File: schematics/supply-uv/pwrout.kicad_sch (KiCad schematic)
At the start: 76 parts, among them Q10 STP13NK60Z, Q11 STP13NK60Z, Q12 IRLML0030, Q7 IRLML0030, Q8 IRLML5203, Q9 IRLML0030, U15 EL817, U16 UC3525, U17 OP213ESZ, U18 IRS21867S, U19 EL817, U20 INA169

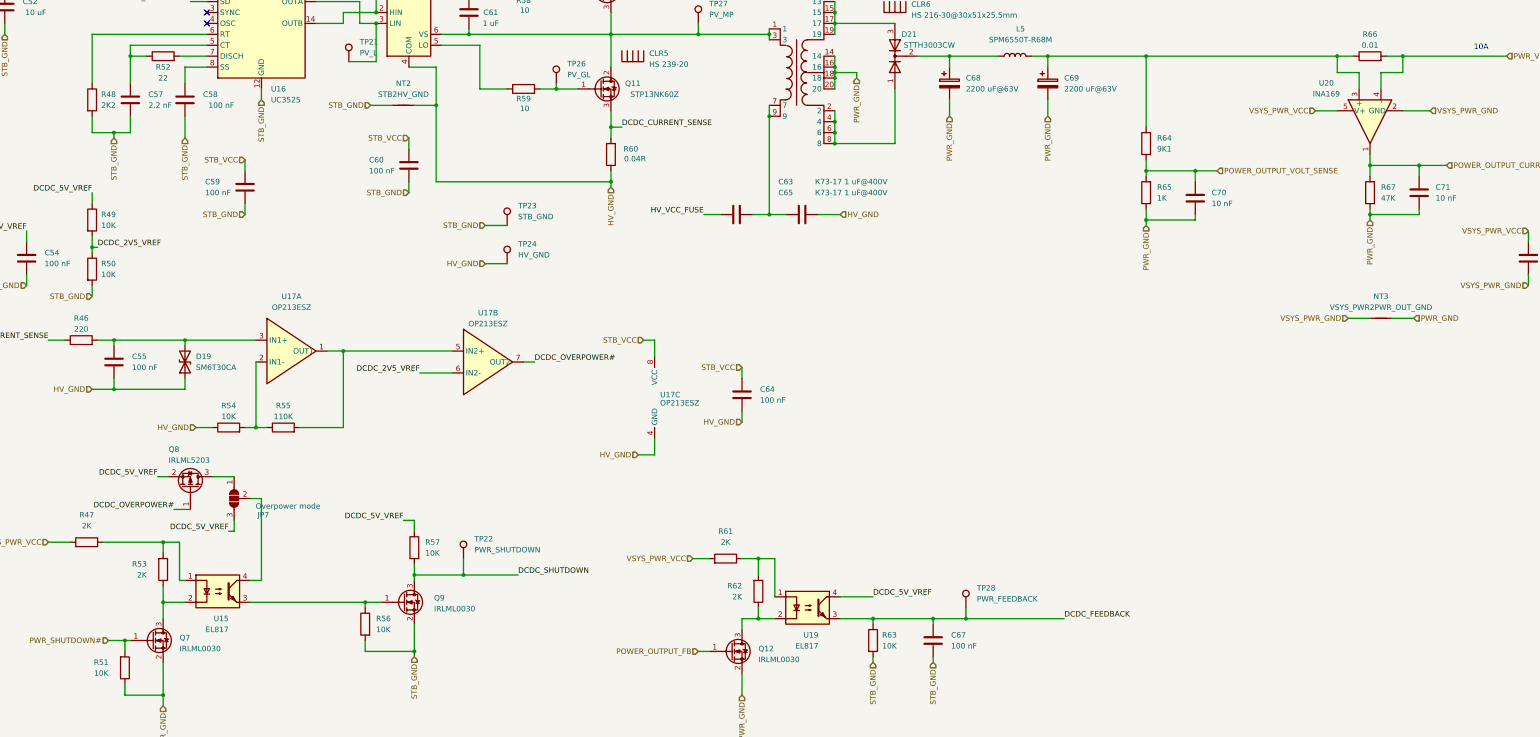
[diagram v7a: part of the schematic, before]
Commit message: power board works (except power output driver, not tested yet), I ready to solder control board
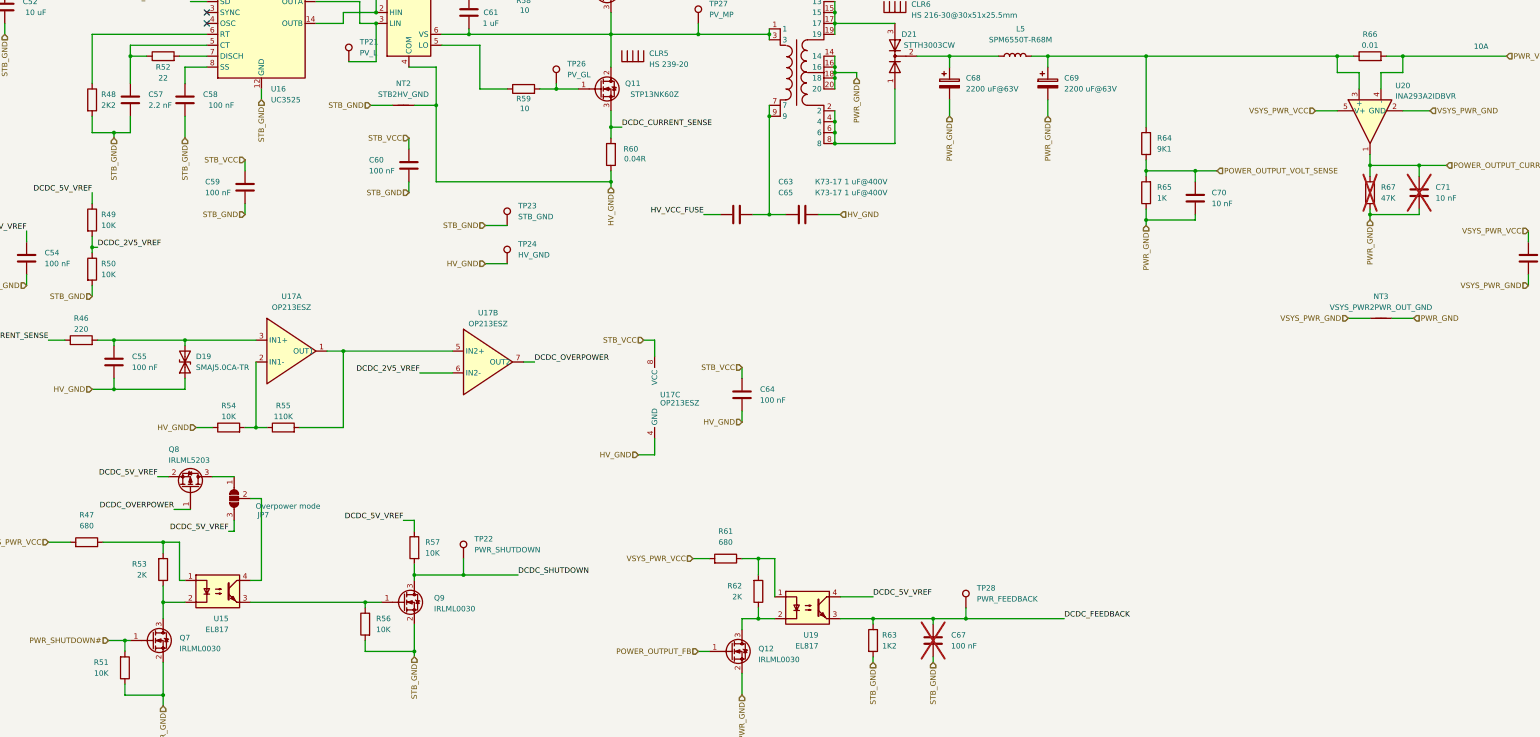
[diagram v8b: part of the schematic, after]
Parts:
- C67, C71, R67: now not fitted
- D19: value SM6T30CA -> SMAJ5.0CA-TR
- R47, R61: value 2K -> 680
- R63: value 10K -> 1K2
- U20: value INA169 -> INA293A2IDBVR
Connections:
- net DCDC_OVERPOWER# renamed DCDC_OVERPOWER
